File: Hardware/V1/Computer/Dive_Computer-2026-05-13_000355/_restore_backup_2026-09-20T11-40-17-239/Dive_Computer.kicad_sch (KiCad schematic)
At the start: 35 parts, among them IC1 LTC4120EUD-4.2#PBF, IC2 MS583730BA01-50, J1 SCREEN, Q1 Si2301HDS, U1 ESP32-C3_SUPERMINI_TH, U2 Si7201-03-IV

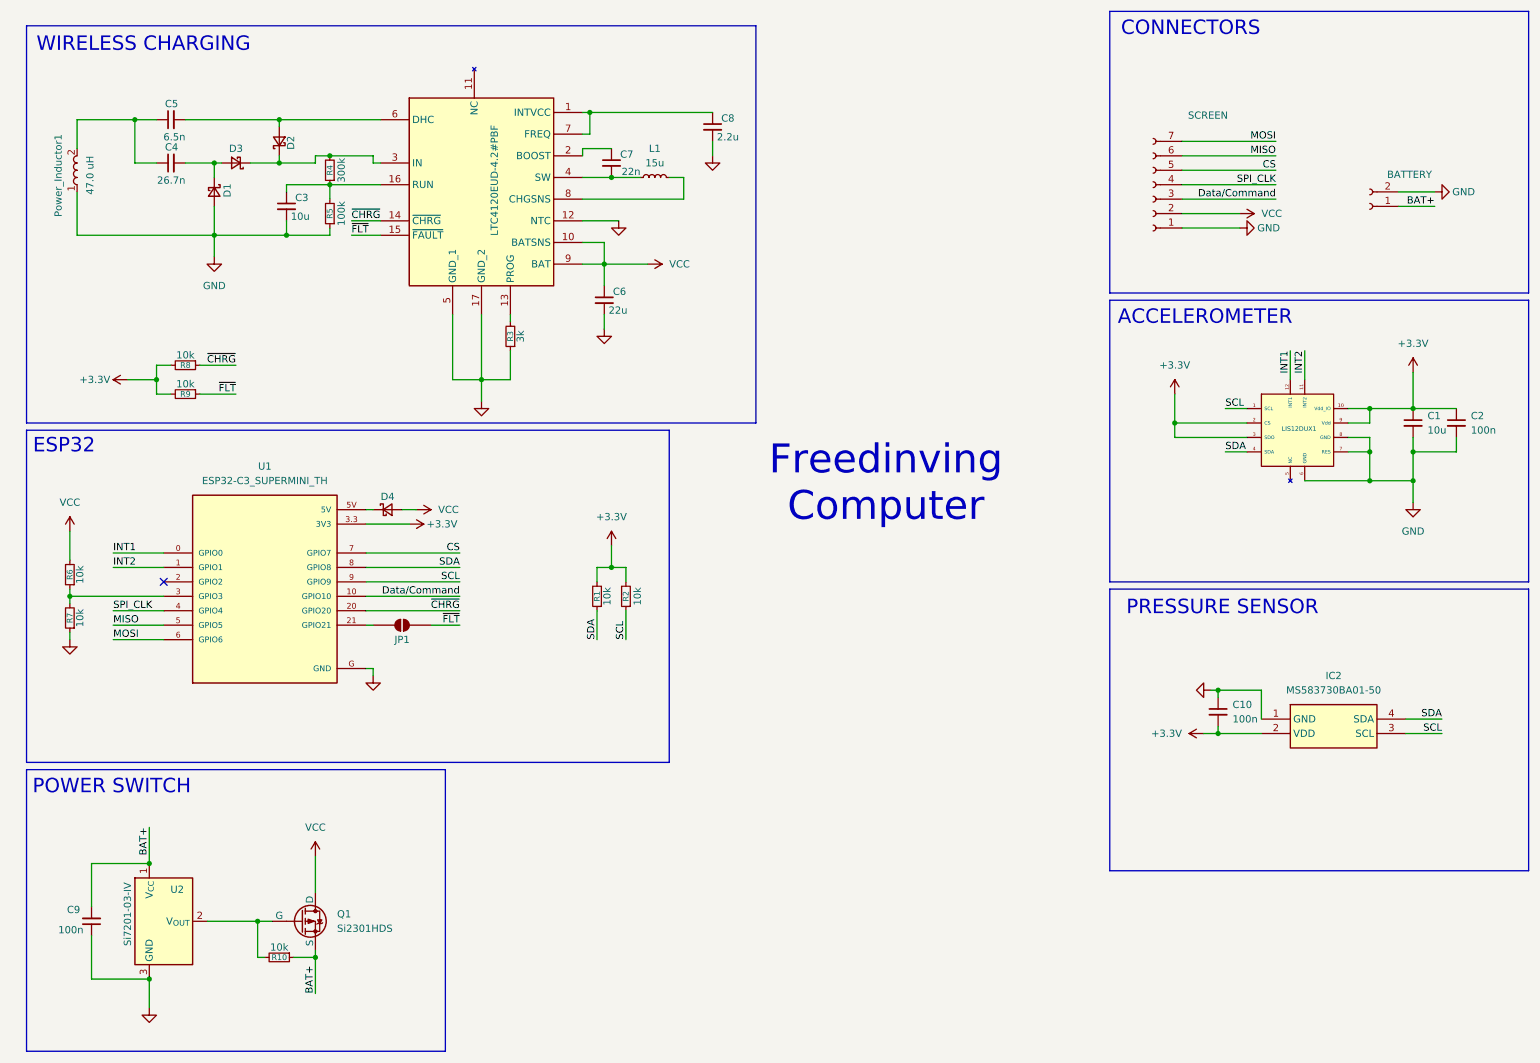
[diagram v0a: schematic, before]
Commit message: added magnetometer & haptic driver
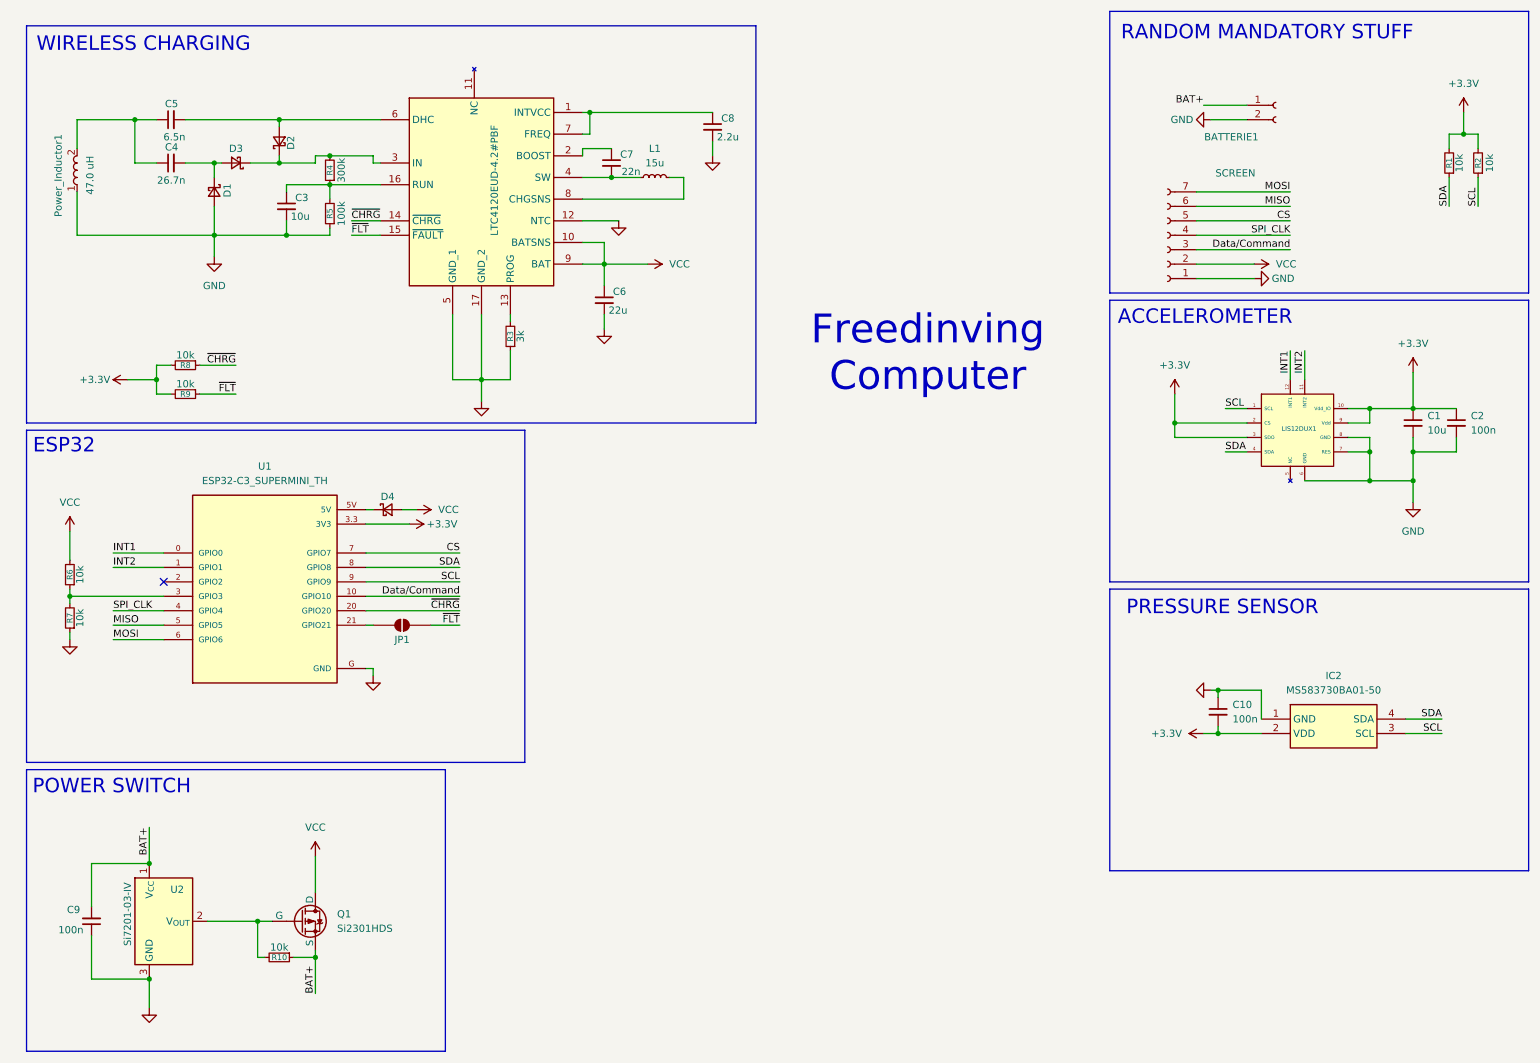
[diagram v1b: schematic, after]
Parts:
- renumbered BATTERY to BATTERIE1
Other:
- note added: "RANDOM MANDATORY STUFF"
- note removed: "CONNECTORS"
- moved on the sheet: BATTERIE1, R1, R2
